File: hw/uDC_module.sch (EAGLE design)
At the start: 34 parts, among them J1 GROVE-4P-2.0-3470130P1, J2 GROVE-4P-2.0-3470130P1, X1 22-23-2021, X2 22-23-2021, X3 53047-06, X4 53047-06

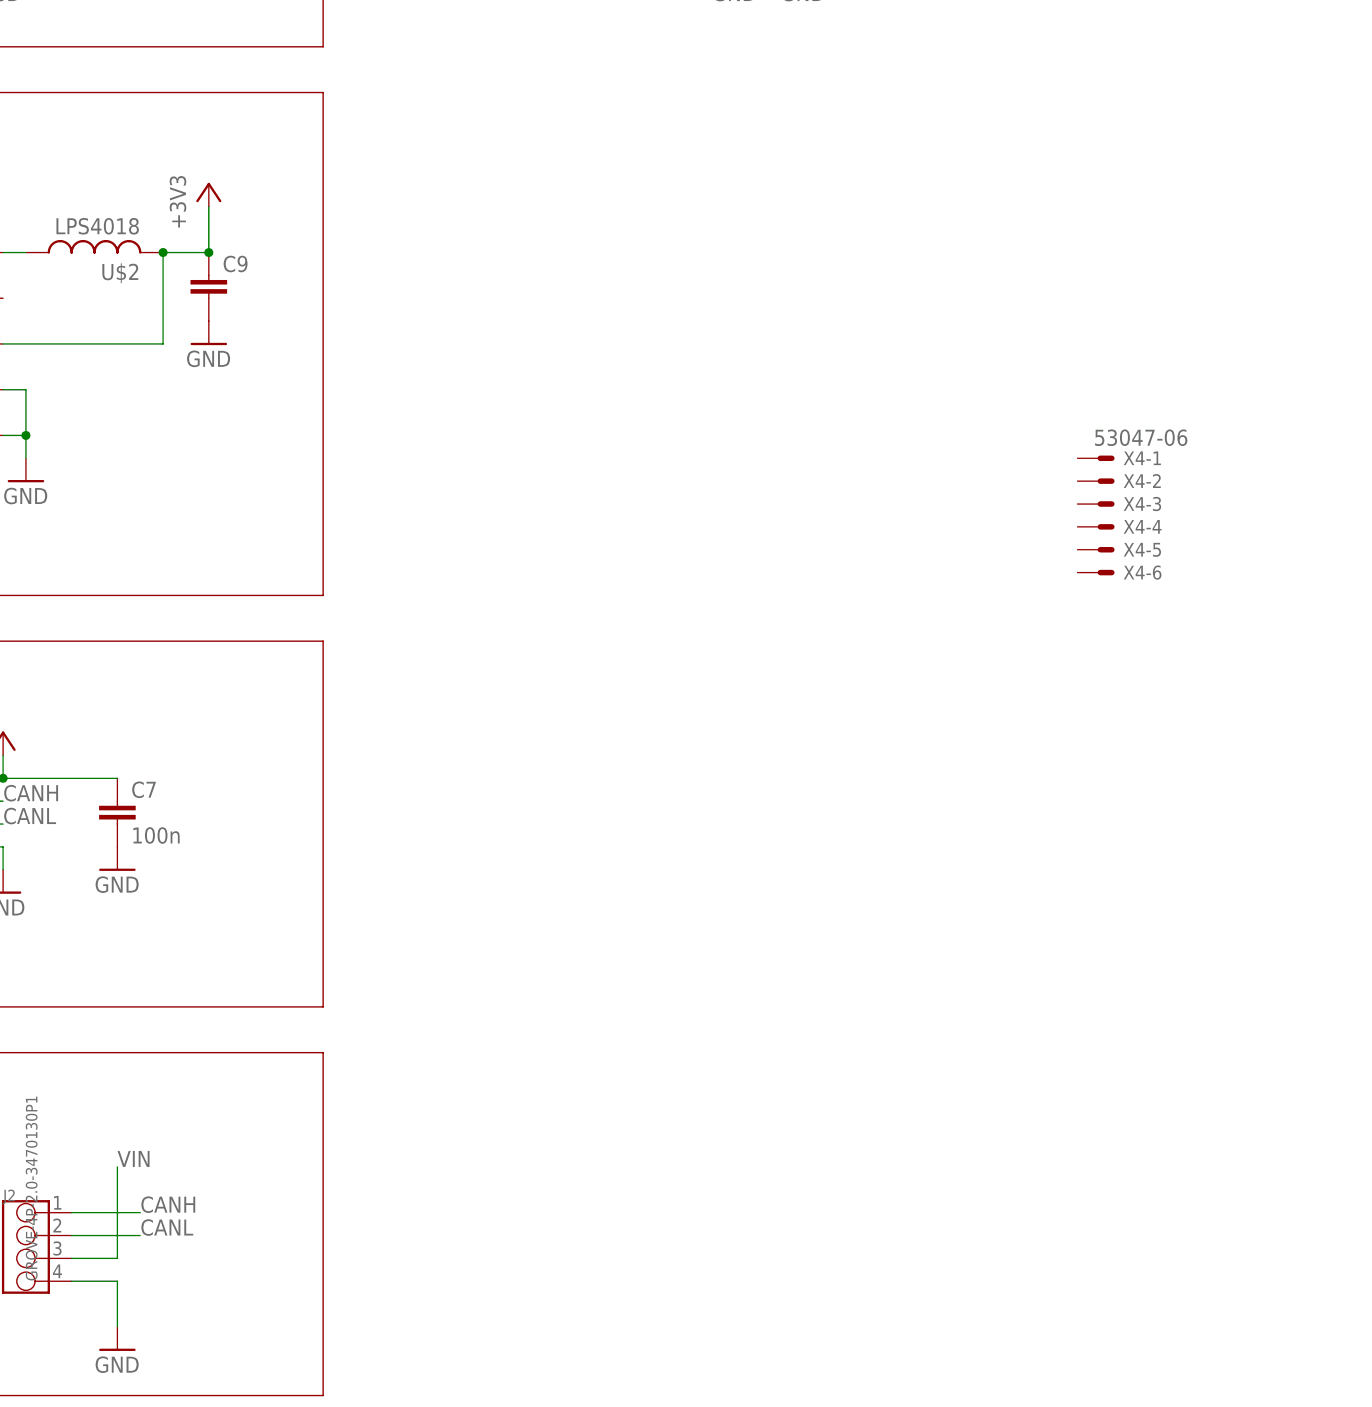
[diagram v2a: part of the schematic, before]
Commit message: working on signal routing
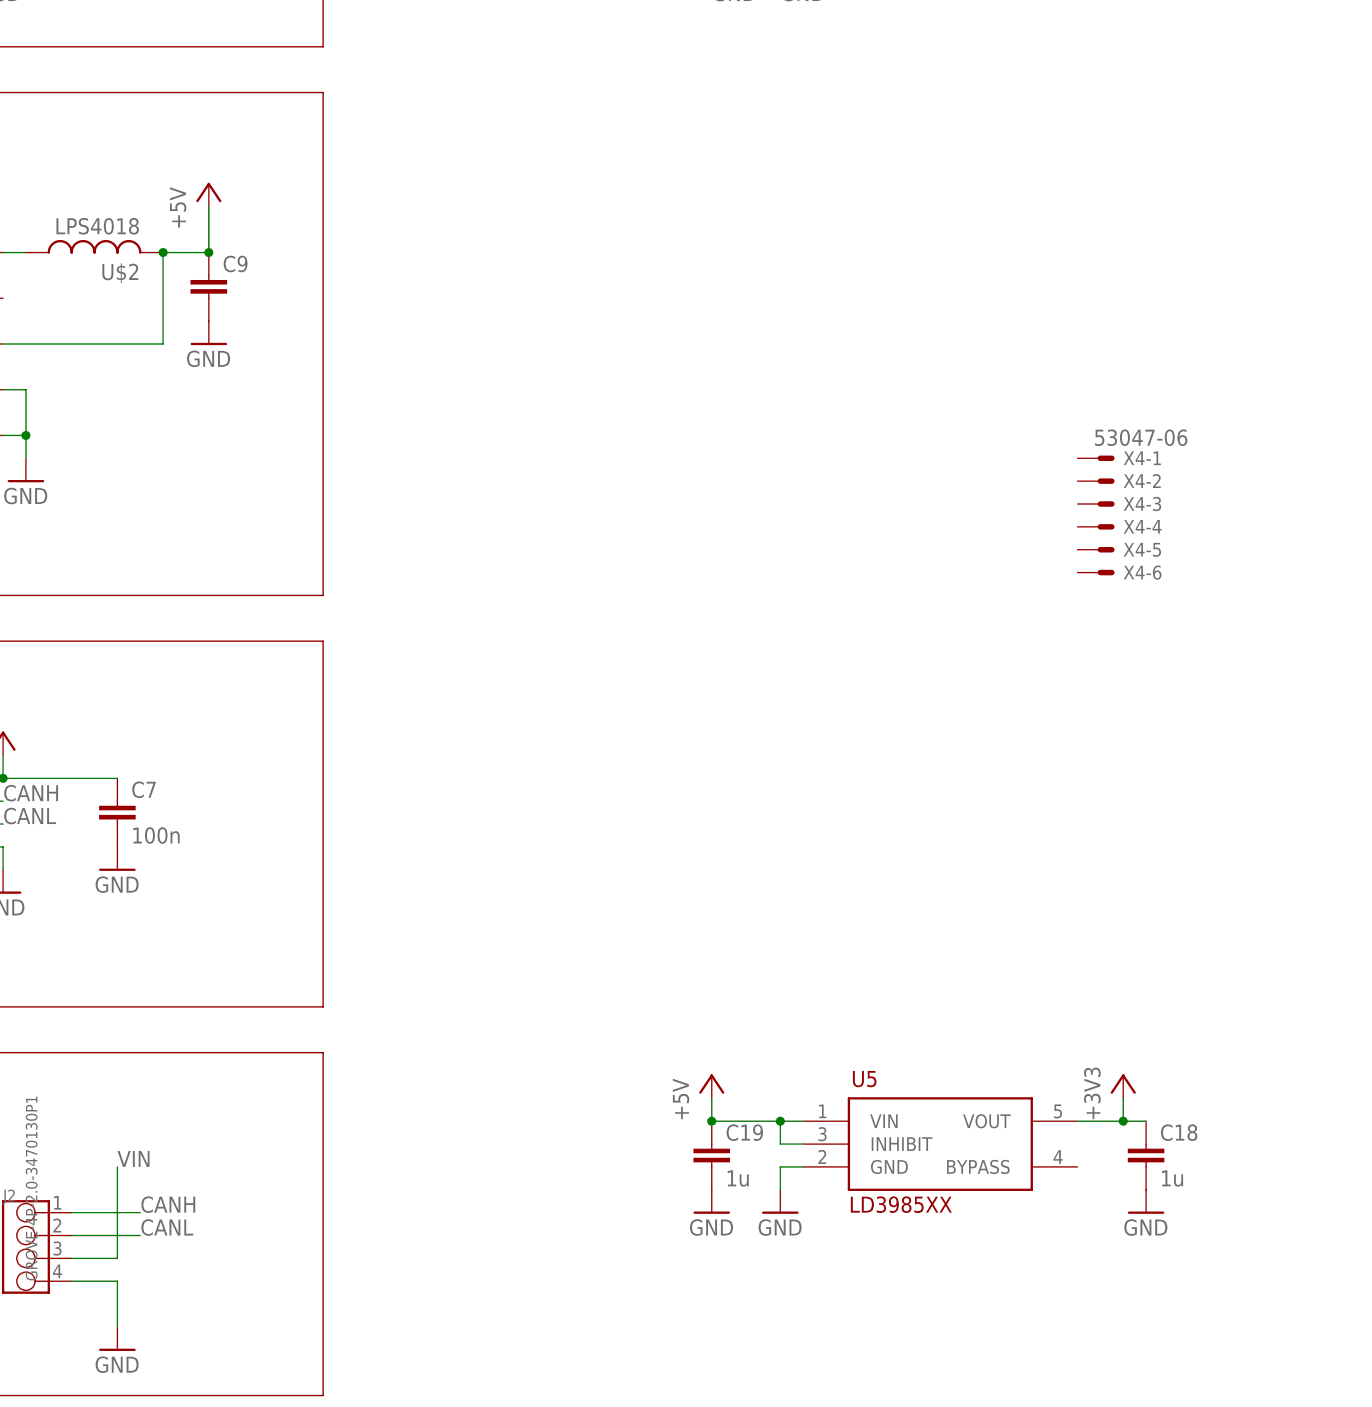
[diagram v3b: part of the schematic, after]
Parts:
- added C18, C19: 1u, rcl:C-EUC0603
- added U5: LD3985XX, st:LD3985XX
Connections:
- new net +5V: C19.1, C9.1, U$2.2, U$3.FB, U5.INHIBIT, U5.VIN
- net +3V3: now also C18.1, U5.VOUT; no longer C9.1, U$2.2, U$3.FB
- net GND: now also C18.2, C19.2, U5.GND
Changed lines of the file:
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@@
 <part name="U$3" library="maxim" deviceset="MAX17501" device=""/>
 <part name="J1" library="OPL Eagle Library" deviceset="GROVE-4P-2.0" device="-3470130P1"/>
-<part name="+3V7" library="supply1" deviceset="+3V3" device=""/>
 <part name="U$6" library="st" deviceset="STM32F103CX" device="TX"/>
 <part name="FRAME1" library="frames" deviceset="DINA3_L" device=""/>
@@
 <part name="GND14" library="supply" deviceset="GND" device=""/>
 <part name="U$7" library="freescale" deviceset="MC33962" device=""/>
+<part name="U5" library="st" deviceset="LD3985XX" device=""/>
+<part name="GND25" library="supply1" deviceset="GND" device=""/>
+<part name="+3V9" library="supply1" deviceset="+3V3" device=""/>
+<part name="C18" library="rcl" deviceset="C-EU" device="C0603" value="1u"/>
+<part name="C19" library="rcl" deviceset="C-EU" device="C0603" value="1u"/>
+<part name="GND26" library="supply1" deviceset="GND" device=""/>
+<part name="GND28" library="supply1" deviceset="GND" device=""/>
+<part name="P+10" library="supply" deviceset="+5V" device=""/>
+<part name="P+3" library="supply" deviceset="+5V" device=""/>
 </parts>
 <sheets>
@@
 <instance part="U$3" gate="G$1" x="96.52" y="121.92"/>
 <instance part="J1" gate="J" x="71.12" y="21.59"/>
-<instance part="+3V7" gate="G$1" x="134.62" y="139.7"/>
 <instance part="U$6" gate="G$1" x="55.88" y="205.74"/>
 <instance part="FRAME1" gate="G$1" x="0" y="0"/>
@@
 <instance part="GND14" gate="1" x="294.64" y="137.16"/>
 <instance part="U$7" gate="G$1" x="223.52" y="185.42"/>
+<instance part="U5" gate="G$1" x="215.9" y="33.02"/>
+<instance part="GND25" gate="1" x="198.12" y="25.4"/>
+<instance part="+3V9" gate="G$1" x="236.22" y="40.64"/>
+<instance part="C18" gate="G$1" x="238.76" y="33.02"/>
+<instance part="C19" gate="G$1" x="190.5" y="33.02"/>
+<instance part="GND26" gate="1" x="190.5" y="25.4"/>
+<instance part="GND28" gate="1" x="238.76" y="25.4"/>
+<instance part="P+10" gate="1" x="190.5" y="40.64"/>
+<instance part="P+3" gate="1" x="134.62" y="139.7"/>
 </instances>
 <busses>
@@
 <pinref part="C11" gate="G$1" pin="-"/>
 <pinref part="GND14" gate="1" pin="GND"/>
+</segment>
+<segment>
+<wire x1="200.66" y1="30.48" x2="198.12" y2="30.48" width="0.1524" layer="91"/>
+<wire x1="198.12" y1="30.48" x2="198.12" y2="27.94" width="0.1524" layer="91"/>
+<pinref part="U5" gate="G$1" pin="GND"/>
+<pinref part="GND25" gate="1" pin="GND"/>
+</segment>
+<segment>
+<pinref part="C19" gate="G$1" pin="2"/>
+<pinref part="GND26" gate="1" pin="GND"/>
+</segment>
+<segment>
+<pinref part="C18" gate="G$1" pin="2"/>
+<pinref part="GND28" gate="1" pin="GND"/>
 </segment>
 </net>
@@
 </segment>
 <segment>
-<wire x1="111.76" y1="121.92" x2="129.54" y2="121.92" width="0.1524" layer="91"/>
-<wire x1="129.54" y1="121.92" x2="129.54" y2="132.08" width="0.1524" layer="91"/>
-<pinref part="U$2" gate="G$1" pin="2"/>
-<wire x1="129.54" y1="132.08" x2="134.62" y2="132.08" width="0.1524" layer="91"/>
-<junction x="129.54" y="132.08"/>
-<pinref part="C9" gate="G$1" pin="1"/>
-<pinref part="U$3" gate="G$1" pin="FB"/>
-<wire x1="134.62" y1="132.08" x2="134.62" y2="137.16" width="0.1524" layer="91"/>
-<junction x="134.62" y="132.08"/>
-<pinref part="+3V7" gate="G$1" pin="+3V3"/>
+<wire x1="231.14" y1="35.56" x2="236.22" y2="35.56" width="0.1524" layer="91"/>
+<wire x1="236.22" y1="35.56" x2="236.22" y2="38.1" width="0.1524" layer="91"/>
+<wire x1="236.22" y1="35.56" x2="238.76" y2="35.56" width="0.1524" layer="91"/>
+<junction x="236.22" y="35.56"/>
+<pinref part="U5" gate="G$1" pin="VOUT"/>
+<pinref part="+3V9" gate="G$1" pin="+3V3"/>
+<pinref part="C18" gate="G$1" pin="1"/>
 </segment>
 </net>
@@
 </segment>
 </net>
+<net name="+5V" class="0">
+<segment>
+<pinref part="U5" gate="G$1" pin="VIN"/>
+<pinref part="C19" gate="G$1" pin="1"/>
+<wire x1="190.5" y1="35.56" x2="198.12" y2="35.56" width="0.1524" layer="91"/>
+<pinref part="U5" gate="G$1" pin="INHIBIT"/>
+<wire x1="198.12" y1="35.56" x2="200.66" y2="35.56" width="0.1524" layer="91"/>
+<wire x1="200.66" y1="33.02" x2="198.12" y2="33.02" width="0.1524" layer="91"/>
+<wire x1="198.12" y1="33.02" x2="198.12" y2="35.56" width="0.1524" layer="91"/>
+<junction x="198.12" y="35.56"/>
+<pinref part="P+10" gate="1" pin="+5V"/>
+<wire x1="190.5" y1="38.1" x2="190.5" y2="35.56" width="0.1524" layer="91"/>
+<junction x="190.5" y="35.56"/>
+</segment>
+<segment>
+<wire x1="111.76" y1="121.92" x2="129.54" y2="121.92" width="0.1524" layer="91"/>
+<wire x1="129.54" y1="121.92" x2="129.54" y2="132.08" width="0.1524" layer="91"/>
+<pinref part="U$2" gate="G$1" pin="2"/>
+<wire x1="129.54" y1="132.08" x2="134.62" y2="132.08" width="0.1524" layer="91"/>
+<junction x="129.54" y="132.08"/>
+<pinref part="C9" gate="G$1" pin="1"/>
+<pinref part="U$3" gate="G$1" pin="FB"/>
+<wire x1="134.62" y1="132.08" x2="134.62" y2="137.16" width="0.1524" layer="91"/>
+<junction x="134.62" y="132.08"/>
+<pinref part="P+3" gate="1" pin="+5V"/>
+</segment>
+</net>

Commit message: working on signal routin
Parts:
- added ZD1: (no value), dp_devices:ZENERSOD-323F
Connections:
- removed net INV: U$7.INV
- net !D2: now also U$6.PA12
- net !SF: now also U$6.PA10
- net D1: now also U$6.PA11
- net EN: now also U$6.PB0
- net FB: now also U$6.PB1, ZD1.C
- net GND: now also ZD1.A
- net IN1: now also U$6.PB13
- net IN2: now also U$6.PA8
- net SLEW: now also U$6.PB12
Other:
- moved on the sheet: C15, R2
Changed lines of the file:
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@@
 <part name="P+10" library="supply" deviceset="+5V" device=""/>
 <part name="P+3" library="supply" deviceset="+5V" device=""/>
+<part name="ZD1" library="dp_devices" deviceset="ZENER" device="SOD-323F"/>
+<part name="GND27" library="supply" deviceset="GND" device=""/>
 </parts>
 <sheets>
@@
 <instance part="C13" gate="G$1" x="284.48" y="144.78"/>
 <instance part="GND21" gate="1" x="284.48" y="137.16"/>
-<instance part="C15" gate="G$1" x="200.66" y="172.72"/>
-<instance part="R2" gate="G$1" x="193.04" y="170.18" rot="R90"/>
-<instance part="GND23" gate="1" x="200.66" y="162.56"/>
-<instance part="GND24" gate="1" x="193.04" y="162.56"/>
+<instance part="C15" gate="G$1" x="195.58" y="172.72"/>
+<instance part="R2" gate="G$1" x="187.96" y="170.18" rot="R90"/>
+<instance part="GND23" gate="1" x="195.58" y="162.56"/>
+<instance part="GND24" gate="1" x="187.96" y="162.56"/>
 <instance part="X4" gate="-1" x="233.68" y="109.22"/>
 <instance part="X4" gate="-2" x="233.68" y="106.68"/>
@@
 <instance part="P+10" gate="1" x="190.5" y="40.64"/>
 <instance part="P+3" gate="1" x="134.62" y="139.7"/>
+<instance part="ZD1" gate="G$1" x="180.34" y="170.18" rot="R90"/>
+<instance part="GND27" gate="1" x="180.34" y="162.56"/>
 </instances>
 <busses>
@@
 <pinref part="C15" gate="G$1" pin="2"/>
 <pinref part="GND23" gate="1" pin="GND"/>
-<wire x1="200.66" y1="165.1" x2="200.66" y2="167.64" width="0.1524" layer="91"/>
+<wire x1="195.58" y1="165.1" x2="195.58" y2="167.64" width="0.1524" layer="91"/>
 </segment>
 <segment>
@@
 <pinref part="C18" gate="G$1" pin="2"/>
 <pinref part="GND28" gate="1" pin="GND"/>
+</segment>
+<segment>
+<pinref part="ZD1" gate="G$1" pin="A"/>
+<pinref part="GND27" gate="1" pin="GND"/>
+<wire x1="180.34" y1="167.64" x2="180.34" y2="165.1" width="0.1524" layer="91"/>
 </segment>
 </net>
@@
 <segment>
 <wire x1="63.5" y1="177.8" x2="63.5" y2="175.26" width="0.1524" layer="91"/>
-<label x="63.5" y="170.18" size="1.778" layer="95" rot="R90"/>
+<label x="63.5" y="175.26" size="1.778" layer="95" rot="MR270"/>
 <pinref part="U$6" gate="G$1" pin="PA13"/>
 </segment>
@@
 <segment>
 <wire x1="66.04" y1="177.8" x2="66.04" y2="175.26" width="0.1524" layer="91"/>
-<label x="66.04" y="170.18" size="1.778" layer="95" rot="R90"/>
+<label x="66.04" y="175.26" size="1.778" layer="95" rot="MR270"/>
 <pinref part="U$6" gate="G$1" pin="PA14"/>
 </segment>
@@
 <segment>
 <wire x1="68.58" y1="177.8" x2="68.58" y2="175.26" width="0.1524" layer="91"/>
-<label x="68.58" y="170.18" size="1.778" layer="95" rot="R90"/>
+<label x="68.58" y="175.26" size="1.778" layer="95" rot="MR270"/>
 <pinref part="U$6" gate="G$1" pin="PA15"/>
 </segment>
@@
 <net name="FB" class="0">
 <segment>
-<wire x1="205.74" y1="175.26" x2="200.66" y2="175.26" width="0.1524" layer="91"/>
+<wire x1="205.74" y1="175.26" x2="195.58" y2="175.26" width="0.1524" layer="91"/>
 <pinref part="C15" gate="G$1" pin="1"/>
-<wire x1="200.66" y1="175.26" x2="193.04" y2="175.26" width="0.1524" layer="91"/>
-<junction x="200.66" y="175.26"/>
+<wire x1="195.58" y1="175.26" x2="187.96" y2="175.26" width="0.1524" layer="91"/>
+<junction x="195.58" y="175.26"/>
 <pinref part="R2" gate="G$1" pin="2"/>
-<wire x1="193.04" y1="175.26" x2="187.96" y2="175.26" width="0.1524" layer="91"/>
-<junction x="193.04" y="175.26"/>
-<label x="187.96" y="175.26" size="1.778" layer="95" rot="MR0"/>
+<wire x1="187.96" y1="175.26" x2="180.34" y2="175.26" width="0.1524" layer="91"/>
+<junction x="187.96" y="175.26"/>
+<label x="175.26" y="175.26" size="1.778" layer="95" rot="MR0"/>
 <pinref part="U$7" gate="G$1" pin="FB"/>
+<pinref part="ZD1" gate="G$1" pin="C"/>
+<wire x1="180.34" y1="175.26" x2="175.26" y2="175.26" width="0.1524" layer="91"/>
+<wire x1="180.34" y1="172.72" x2="180.34" y2="175.26" width="0.1524" layer="91"/>
+<junction x="180.34" y="175.26"/>
+</segment>
+<segment>
+<pinref part="U$6" gate="G$1" pin="PB1"/>
+<wire x1="83.82" y1="195.58" x2="86.36" y2="195.58" width="0.1524" layer="91"/>
+<label x="86.36" y="195.58" size="1.778" layer="95"/>
 </segment>
 </net>
 <net name="!SF" class="0">
 <segment>
-<wire x1="205.74" y1="177.8" x2="203.2" y2="177.8" width="0.1524" layer="91"/>
-<label x="203.2" y="177.8" size="1.778" layer="95" rot="MR0"/>
+<wire x1="205.74" y1="177.8" x2="200.66" y2="177.8" width="0.1524" layer="91"/>
+<label x="200.66" y="177.8" size="1.778" layer="95" rot="MR0"/>
 <pinref part="U$7" gate="G$1" pin="!SF"/>
 </segment>
+<segment>
+<pinref part="U$6" gate="G$1" pin="PA10"/>
+<wire x1="55.88" y1="177.8" x2="55.88" y2="175.26" width="0.1524" layer="91"/>
+<label x="55.88" y="175.26" size="1.778" layer="95" rot="MR270"/>
+</segment>
 </net>
 <net name="SLEW" class="0">
 <segment>
-<wire x1="205.74" y1="180.34" x2="203.2" y2="180.34" width="0.1524" layer="91"/>
-<label x="203.2" y="180.34" size="1.778" layer="95" rot="MR0"/>
+<wire x1="205.74" y1="180.34" x2="200.66" y2="180.34" width="0.1524" layer="91"/>
+<label x="200.66" y="180.34" size="1.778" layer="95" rot="MR0"/>
 <pinref part="U$7" gate="G$1" pin="SLEW"/>
 </segment>
-</net>
-<net name="INV" class="0">
-<segment>
-<wire x1="205.74" y1="182.88" x2="203.2" y2="182.88" width="0.1524" layer="91"/>
-<label x="203.2" y="182.88" size="1.778" layer="95" rot="MR0"/>
-<pinref part="U$7" gate="G$1" pin="INV"/>
-</segment>
-</net>
-<net name="D1" class="0">
-<segment>
-<wire x1="205.74" y1="185.42" x2="203.2" y2="185.42" width="0.1524" layer="91"/>
-<label x="203.2" y="185.42" size="1.778" layer="95" rot="MR0"/>
-<pinref part="U$7" gate="G$1" pin="D1"/>
+<segment>
+<pinref part="U$6" gate="G$1" pin="PB12"/>
+<wire x1="68.58" y1="236.22" x2="68.58" y2="238.76" width="0.1524" layer="91"/>
+<label x="68.58" y="238.76" size="1.778" layer="95" rot="R90"/>
 </segment>
 </net>
 <net name="!D2" class="0">
 <segment>
-<wire x1="205.74" y1="187.96" x2="203.2" y2="187.96" width="0.1524" layer="91"/>
-<label x="203.2" y="187.96" size="1.778" layer="95" rot="MR0"/>
+<wire x1="205.74" y1="187.96" x2="200.66" y2="187.96" width="0.1524" layer="91"/>
+<label x="200.66" y="187.96" size="1.778" layer="95" rot="MR0"/>
 <pinref part="U$7" gate="G$1" pin="!D2"/>
 </segment>
+<segment>
+<pinref part="U$6" gate="G$1" pin="PA12"/>
+<wire x1="60.96" y1="177.8" x2="60.96" y2="175.26" width="0.1524" layer="91"/>
+<label x="60.96" y="175.26" size="1.778" layer="95" rot="MR270"/>
+</segment>
 </net>
 <net name="IN2" class="0">
 <segment>
-<wire x1="205.74" y1="190.5" x2="203.2" y2="190.5" width="0.1524" layer="91"/>
-<label x="203.2" y="190.5" size="1.778" layer="95" rot="MR0"/>
+<wire x1="205.74" y1="190.5" x2="200.66" y2="190.5" width="0.1524" layer="91"/>
+<label x="200.66" y="190.5" size="1.778" layer="95" rot="MR0"/>
 <pinref part="U$7" gate="G$1" pin="IN2"/>
 </segment>
+<segment>
+<pinref part="U$6" gate="G$1" pin="PA8"/>
+<wire x1="50.8" y1="177.8" x2="50.8" y2="175.26" width="0.1524" layer="91"/>
+<label x="50.8" y="175.26" size="1.778" layer="95" rot="MR270"/>
+</segment>
 </net>
 <net name="IN1" class="0">
 <segment>
-<wire x1="205.74" y1="193.04" x2="203.2" y2="193.04" width="0.1524" layer="91"/>
-<label x="203.2" y="193.04" size="1.778" layer="95" rot="MR0"/>
+<wire x1="205.74" y1="193.04" x2="200.66" y2="193.04" width="0.1524" layer="91"/>
+<label x="200.66" y="193.04" size="1.778" layer="95" rot="MR0"/>
 <pinref part="U$7" gate="G$1" pin="IN1"/>
 </segment>
+<segment>
+<pinref part="U$6" gate="G$1" pin="PB13"/>
+<wire x1="66.04" y1="236.22" x2="66.04" y2="238.76" width="0.1524" layer="91"/>
+<label x="66.04" y="238.76" size="1.778" layer="95" rot="R90"/>
+</segment>
 </net>
 <net name="EN" class="0">
 <segment>
-<wire x1="205.74" y1="195.58" x2="203.2" y2="195.58" width="0.1524" layer="91"/>
-<label x="203.2" y="195.58" size="1.778" layer="95" rot="MR0"/>
+<wire x1="205.74" y1="195.58" x2="200.66" y2="195.58" width="0.1524" layer="91"/>
+<label x="200.66" y="195.58" size="1.778" layer="95" rot="MR0"/>
 <pinref part="U$7" gate="G$1" pin="EN"/>
+</segment>
+<segment>
+<pinref part="U$6" gate="G$1" pin="PB0"/>
+<wire x1="83.82" y1="193.04" x2="86.36" y2="193.04" width="0.1524" layer="91"/>
+<label x="86.36" y="193.04" size="1.778" layer="95"/>
 </segment>
 </net>
@@
 </segment>
 </net>
+<net name="D1" class="0">
+<segment>
+<pinref part="U$7" gate="G$1" pin="D1"/>
+<wire x1="200.66" y1="185.42" x2="205.74" y2="185.42" width="0.1524" layer="91"/>
+<label x="200.66" y="185.42" size="1.778" layer="95" rot="MR0"/>
+</segment>
+<segment>
+<pinref part="U$6" gate="G$1" pin="PA11"/>
+<wire x1="58.42" y1="177.8" x2="58.42" y2="175.26" width="0.1524" layer="91"/>
+<label x="58.42" y="175.26" size="1.778" layer="95" rot="MR270"/>
+</segment>
+</net>
